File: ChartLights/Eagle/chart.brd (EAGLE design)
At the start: 53 x 59.7 mm, 8 parts, among them J0 0, J1 0, U0 TLC5916IN, U1 TLC5916IN

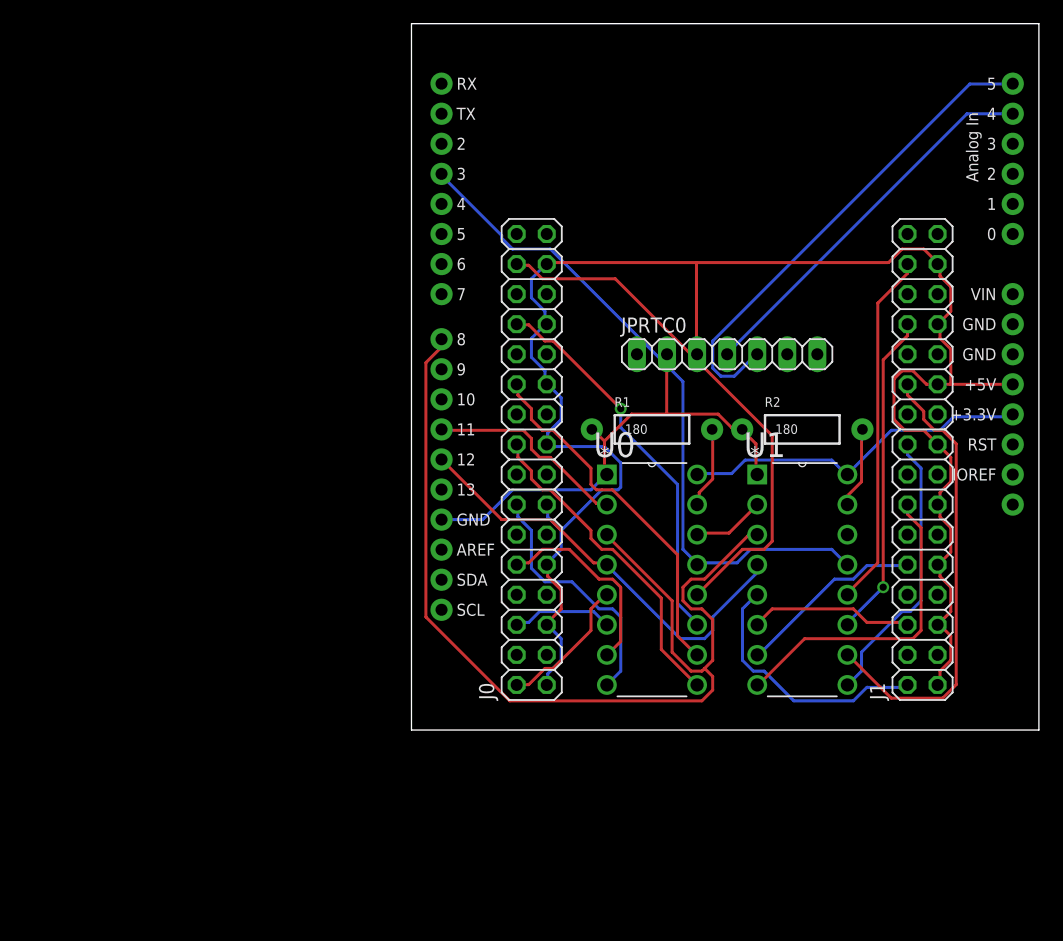
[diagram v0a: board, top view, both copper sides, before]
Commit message: 2x20 headers x2, all on one UnoR3 header
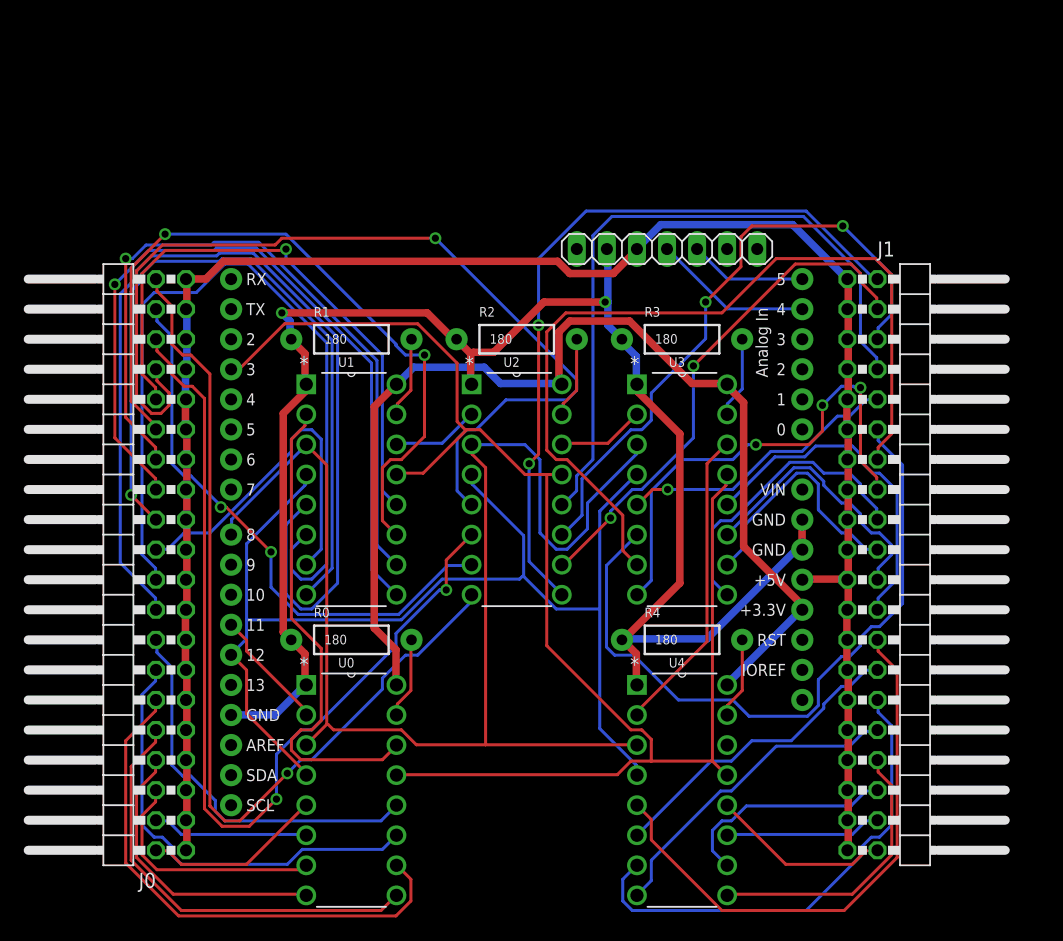
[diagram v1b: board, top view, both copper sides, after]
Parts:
- added R0, R3, R4: 180, SparkFun-Resistors:AXIAL-0.4
- added U2, U3, U4: TLC5916IN, Texas Instruments_By_element14_Batch_1:DIP254P762X508-16
- J0, J1: value 0 -> 2x20; device pinhead:2X16 -> pinhead:2X20/90
- moved U1 38.9 mm to (25.4, 27.9)
- moved J0 36.7 mm to (1.27, 30.5)
- moved U0 31.0 mm to (25.4, 2.54)
- moved R1 26.5 mm to (21.6, 49.5)
- moved R2 25.3 mm to (35.6, 49.5)
- moved B0 24.3 mm to (8.89, 0.00)
- moved JPRTC0 10.2 mm to (48.3, 57.1)
- moved J1 8.89 mm to (69.8, 30.5), turned to 270 degrees
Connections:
- new net DATA3: U2.14, U3.2
- new net DATA4: U3.14, U4.2
- new net DATA5: U4.14
- new net L2-0: J0.34, U2.5
- new net L2-1: J0.36, U2.6
- new net L2-2: J0.38, U2.7
- new net L2-3: J0.40, U2.8
- new net L2-4: J1.2, U2.9
- new net L2-5: J1.4, U2.10
- new net L2-6: J1.6, U2.11
- new net L2-7: J1.8, U2.12
- new net L3-0: J1.10, U3.5
- new net L3-1: J1.12, U3.6
- new net L3-2: J1.14, U3.7
- new net L3-3: J1.16, U3.8
- new net L3-4: J1.18, U3.9
- new net L3-5: J1.20, U3.10
- new net L3-6: J1.22, U3.11
- new net L3-7: J1.24, U3.12
- new net L4-0: J1.26, U4.5
- new net L4-1: J1.28, U4.6
- new net L4-2: J1.30, U4.7
- new net L4-3: J1.32, U4.8
- new net L4-4: J1.34, U4.9
- new net L4-5: J1.36, U4.10
- new net L4-6: J1.38, U4.11
- new net L4-7: J1.40, U4.12
- new net N$2: R2.P$2, U2.15
- new net N$3: R3.P$2, U3.15
- new net N$4: R4.P$2, U4.15
- net DATA2: now also U2.2
- net GND: now also B0.GND@0, B0.GND@1, R0.P$1, R3.P$1, R4.P$1, U2.1, U3.1, U4.1
- net L0-1: now also J0.4; no longer J0.6
- net L0-2: now also J0.6; no longer J0.10
- net L0-3: now also J0.8; no longer J0.14
- net L0-4: now also J0.10; no longer J0.18
- net L0-5: now also J0.12; no longer J0.22
- net L0-6: now also J0.14; no longer J0.26
- net L0-7: now also J0.16; no longer J0.30
- net L1-0: now also J0.18; no longer J1.2
- net L1-1: now also J0.20; no longer J1.6
- net L1-2: now also J0.22; no longer J1.10
- net L1-3: now also J0.24; no longer J1.14
- net L1-4: now also J0.26; no longer J1.18
- net L1-5: now also J0.28; no longer J1.22
- net L1-6: now also J0.30; no longer J1.26
- net L1-7: now also J0.32; no longer J1.30
- net LATCH: now also U2.4, U3.4, U4.4
- net N$1: now also R1.P$2; no longer R2.P$2
- net N$6: now also R0.P$2; no longer R1.P$2
- net PWM: now also U2.13, U3.13, U4.13
- net SCK: now also U2.3, U3.3, U4.3
- net VCC: now also J0.11, J0.15, J0.19, J0.23, J0.27, J0.3, J0.31, J0.33, J0.35, J0.37, J0.39, J0.7, J1.11, J1.15, J1.19, J1.23, J1.27, J1.3, J1.31, J1.33, J1.35, J1.37, J1.39, J1.7
- net VDD: now also U2.16, U3.16, U4.16
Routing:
- net GND: track 42.5 -> 137.7 mm, vias 0 -> 2
- net L2-0: track 0.00 -> 79.9 mm, vias 0 -> 1
- net L2-1: track 0.00 -> 79.5 mm, vias 0 -> 2
- net L2-3: track 0.00 -> 78.2 mm, vias 0 -> 1
- net L3-2: track 0.00 -> 71.7 mm
- net PWM: track 57.6 -> 127.3 mm
- net LATCH: track 36.6 -> 101.7 mm
- net VDD: track 29.8 -> 94.2 mm
- net L1-0: track 22.1 -> 85.8 mm
- net L2-4: track 0.00 -> 62.5 mm, vias 0 -> 2
- net L3-1: track 0.00 -> 59.2 mm
- net L2-7: track 0.00 -> 57.8 mm
- net L1-1: track 14.0 -> 69.5 mm
- net L2-6: track 0.00 -> 52.8 mm, vias 0 -> 2
- net L2-2: track 0.00 -> 47.8 mm, vias 0 -> 2
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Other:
- board outline removed
- board text added: "J0"
- board text added: "J1"
- board text added: "JPRTC0"
- board text added: "R0"
- board text added: "R1"
- board text added: "R2"
- board text added: "R3"
- board text added: "R4"
- board text added: "U0"
- board text added: "U1"
- board text added: "U2"
- board text added: "U3"
- board text added: "U4"
